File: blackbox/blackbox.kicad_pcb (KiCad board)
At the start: 4 copper layers, 55.7 x 46.4 mm, 55 parts, among them J1 Micro_SD_Card_Det2, J2 Conn_01x04_MountingPin, J3 Conn_02x05_Odd_Even, J4 Barrel_Jack_Switch, SW1 SW_SPST, SW2 SW_SPST, U1 STM32C011F4Px, U11 MAX811TEUS-T, U2 HCPL-063A, U3 HCPL-063A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

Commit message: blackbox update
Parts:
- added R13: 10k, Resistor_SMD:R_0805_2012Metric, B.Cu at (212.3, 94.5)
- added R14: 10k, Resistor_SMD:R_0805_2012Metric, B.Cu at (212.3, 87.1)
- R3, R4: value R -> 220R
- Y1: value Crystal_GND24 -> 16Mhz
- moved C17 0.33 mm to (190.0, 85.5)
- moved C1 0.31 mm to (201.0, 95.1)
- moved J2 0.16 mm to (174.8, 71.8)
- moved J1 0.08 mm to (216.4, 92.0)
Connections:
- J1 pad 1: unconnected-(J1-DAT2-Pad1) -> Net-(J1-DAT2)
- J1 pad 8: unconnected-(J1-DAT1-Pad8) -> Net-(J1-DAT1)
- R4 pad 1: Net-(U3-C2) -> Net-(U3-A2)
- R6 pad 2: Net-(U2-C2) -> Net-(U2-A2)
- U2 pad 3: Net-(U2-C2) -> GND1
- U2 pad 4: GND1 -> Net-(U2-A2)
- U3 pad 3: Net-(U3-C2) -> GND
- U3 pad 4: GND -> Net-(U3-A2)
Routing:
- net Net-(U2-A2): track 0.00 -> 7.32 mm
- net Net-(U3-C2): track 7.24 -> 0.00 mm
- net Net-(U2-C2): track 6.08 -> 0.00 mm
- net Net-(U3-A2): track 0.00 -> 5.45 mm
- net Net-(J1-DAT2): track 0.00 -> 2.58 mm, vias 0 -> 1
- net Net-(J1-DAT1): track 0.00 -> 2.54 mm, vias 0 -> 1
- net unconnected-(J2-Pin_3-Pad3): track 2.39 -> 0.00 mm, vias 1 -> 0
- net +3.3V: track 30.4 -> 32.1 mm, vias 12 -> 14
- net GND: track 66.5 -> 67.2 mm

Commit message: Blackbox update
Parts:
- removed BT1: 1051, keys1051:BAT_1051
- added G***: LOGO, shared:logo20x20, B.Cu at (198.1, 85.5)
- added J5: Conn_01x02_MountingPin, Connector_JST:JST_PH_S2B-PH-SM4-TB_1x02-1MP_P2.00mm_Horizontal, F.Cu at (190.9, 70.3)
- added SW3: SW_DPDT_x2, Button_Switch_SMD:SW_DPDT_CK_JS202011JCQN, F.Cu at (200.5, 67.9)
- moved U6 13.3 mm to (220.4, 70.0)
- moved R12 13.2 mm to (223.2, 70.1)
- moved RV1 11.6 mm to (209.7, 68.8)
- moved C12 10.1 mm to (217.2, 70.2), turned to 90 degrees
- moved R7 5.39 mm to (205.1, 72.1), turned to 0 degrees
- moved J4 3.71 mm to (211.2, 78.1)
- moved C15 3.39 mm to (188.4, 76.8), turned to 180 degrees
- moved D4 3.25 mm to (197.4, 72.1)
- moved C7 0.14 mm to (201.9, 72.9)
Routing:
- net Net-(J5-Pin_1): track 0.00 -> 10.3 mm
- net Net-(U4-PRETERM): track 3.74 -> 14.0 mm
- net CHARGER_ISET: track 27.4 -> 36.8 mm
- net GND: track 67.2 -> 74.4 mm, vias 47 -> 45
- net Net-(J4-Pad3): track 8.04 -> 12.7 mm
- net Net-(D4-A): track 2.17 -> 5.43 mm
- net VDD: track 25.8 -> 28.0 mm, vias 10 -> 12
- net Net-(F2-Pad1): track 3.70 -> 5.24 mm
- net Net-(U4-ISET): track 7.20 -> 6.29 mm
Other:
- board text added: "+"
- board text added: "-"
- board text added: "1:RX 2:5V 3:X 4:GND"
- board text added: "BAT"
- board text added: "Charge"
- board text added: "ON"
- board text added: "RST"
- board text added: "UART"

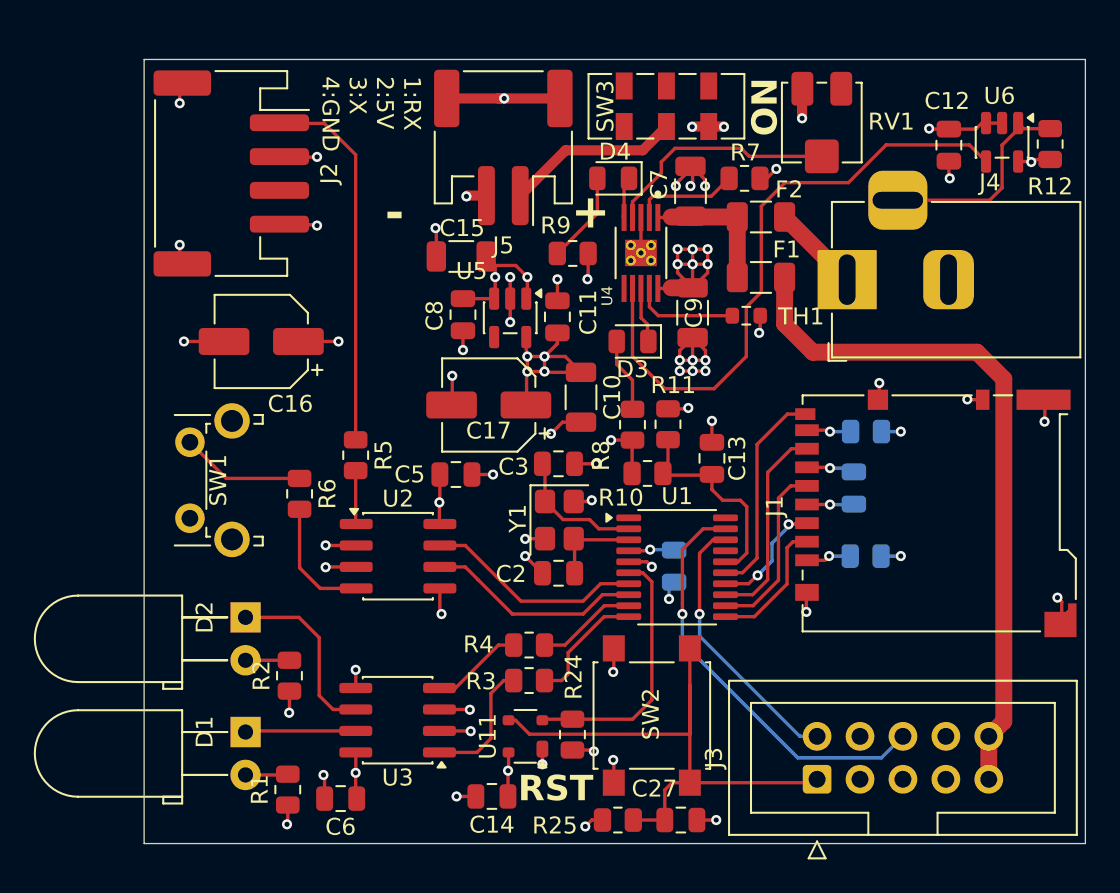
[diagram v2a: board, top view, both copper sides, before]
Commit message: Add NOT gate to fix uart, rework silkscreen
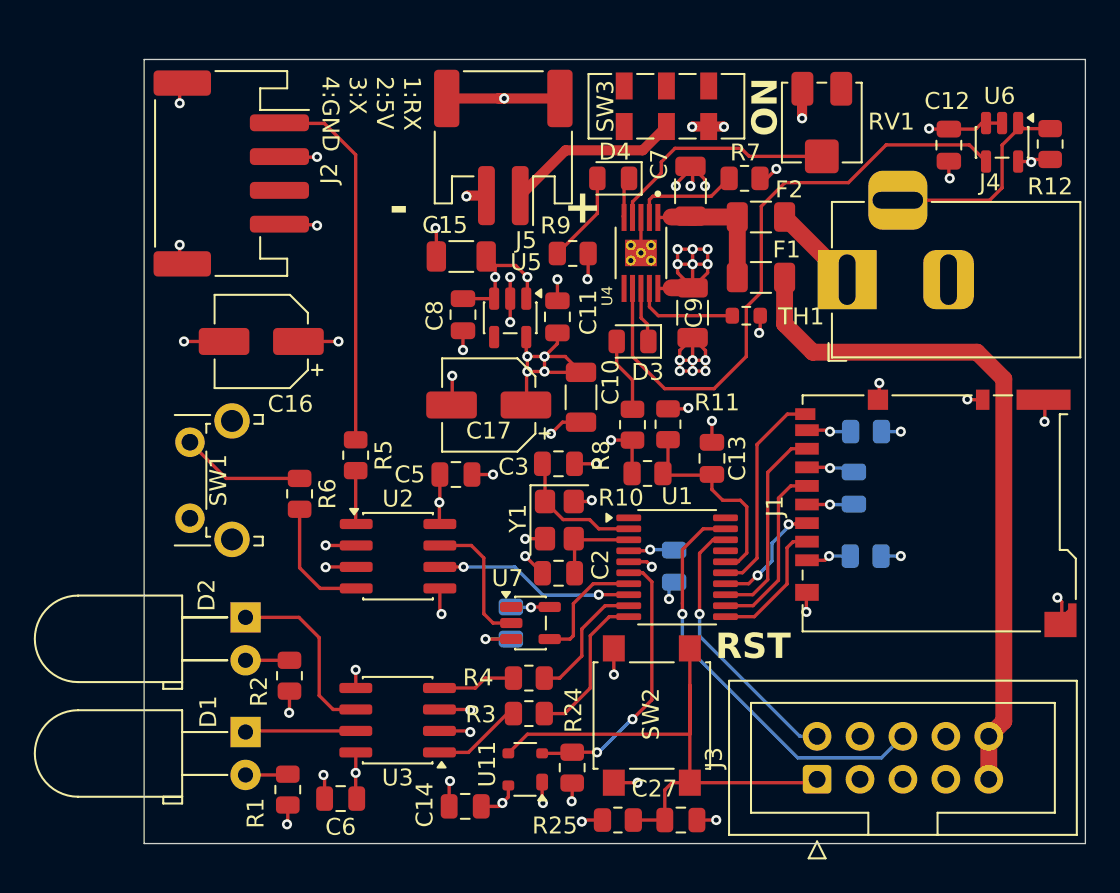
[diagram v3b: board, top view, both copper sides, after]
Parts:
- added C18: 100nF, Capacitor_SMD:C_0805_2012Metric, B.Cu at (191.3, 98.5)
- added U7: 74AHCT1G04, Package_TO_SOT_SMD:SOT-23-5, F.Cu at (192.5, 98.5)
- moved U11 1.96 mm to (192.2, 107.1)
- moved R24 1.96 mm to (194.9, 107.0)
- moved R3 1.96 mm to (192.4, 103.8)
- moved R4 1.96 mm to (192.4, 101.7)
- moved C14 1.69 mm to (188.6, 109.3)
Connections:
- U2 pad 7: ESP_TX -> Net-(U2-VO1)
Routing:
- net Net-(U2-VO1): track 0.00 -> 8.06 mm
- net ESP_TX: track 13.0 -> 7.16 mm
- net GND: track 74.4 -> 78.4 mm, vias 45 -> 46
- net Net-(U3-A1): track 7.72 -> 5.33 mm
- net +3.3V: track 31.7 -> 33.7 mm, vias 14 -> 15
- net LED1: track 7.29 -> 9.19 mm
- net LED2: track 5.95 -> 7.71 mm
- net BUTTON: track 12.8 -> 11.9 mm, vias 0 -> 2
- net Net-(U3-A2): track 5.45 -> 4.62 mm
- net Net-(U1-PF2): track 15.8 -> 16.4 mm, vias 0 -> 2

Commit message: Add more capacitors as SD cards are hungry when hotswapped
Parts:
- added C19: 47uF, Capacitor_SMD:C_1206_3216Metric, B.Cu at (214.1, 90.8)
- added C20: 47uF, Capacitor_SMD:C_1206_3216Metric, F.Cu at (205.7, 85.2)
- added R15: 10K, Resistor_SMD:R_0805_2012Metric, F.Cu at (190.1, 93.3)
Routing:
- net +3.3V: track 33.7 -> 44.4 mm, vias 15 -> 17
- net GND: track 78.4 -> 85.5 mm, vias 46 -> 48
